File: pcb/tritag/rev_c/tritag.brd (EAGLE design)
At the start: 61 x 34.5 mm, 136 parts, among them J1 TC2030-JLINK-NL, J2 TC2030-JLINK-NL, J3 MICRO_USB_B_HIROSE_ZX62-B-5PA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, J5 BAT_HOLE, J7 CON_MICRO_SDDM3AT-SF-PEJM5, T1 HHM1595A1, U1 NRF52840, U12 SIP32510, U2 MCP73831, U3 FT232RQ, U4 MAX8887EZK33+T, U5 STM32F091CC, U6 SKY13317, U7 LXDC2HN18A, U8 DW1000, U9 LIS2DW12, X1 32MHz, X2 38.4M, X3 16M, X4 32.768kHz

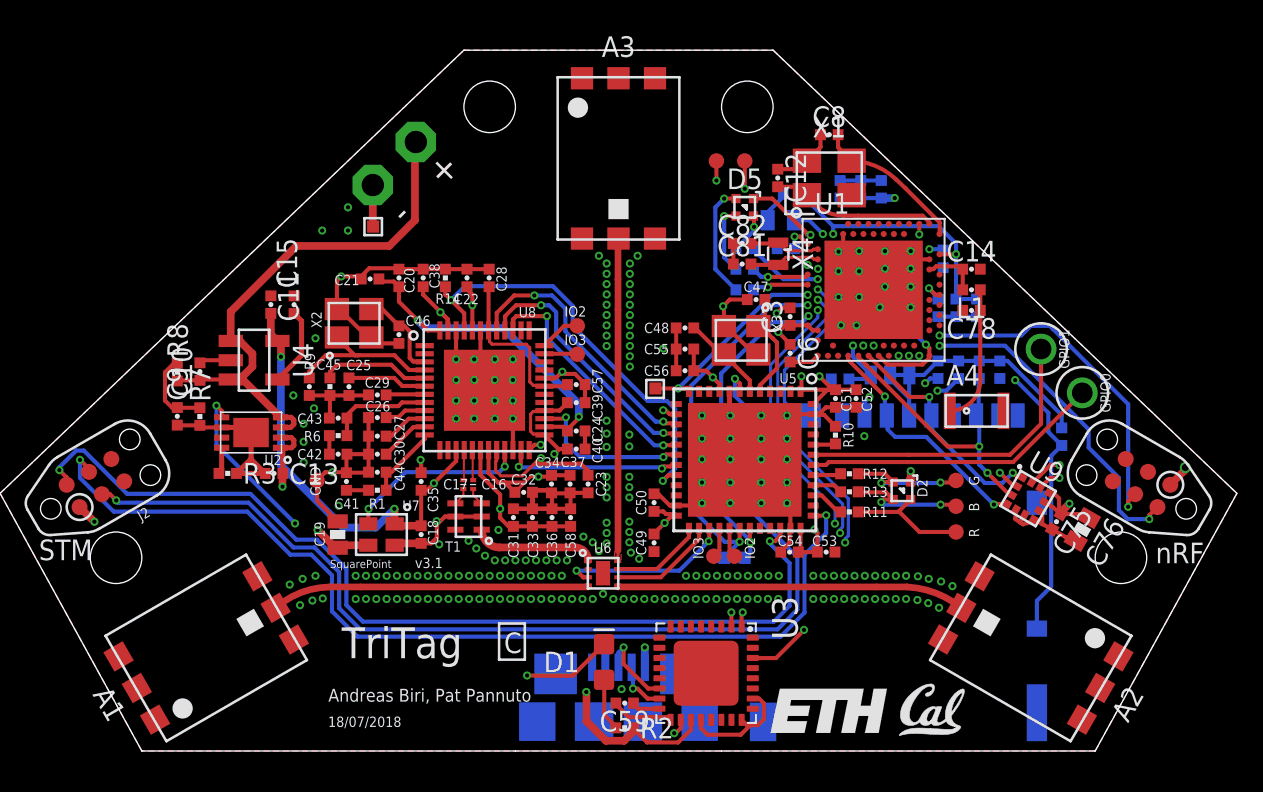
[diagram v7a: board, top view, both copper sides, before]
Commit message: added antenna keepout, improved power distribution and ground coverage plus RF for nRF
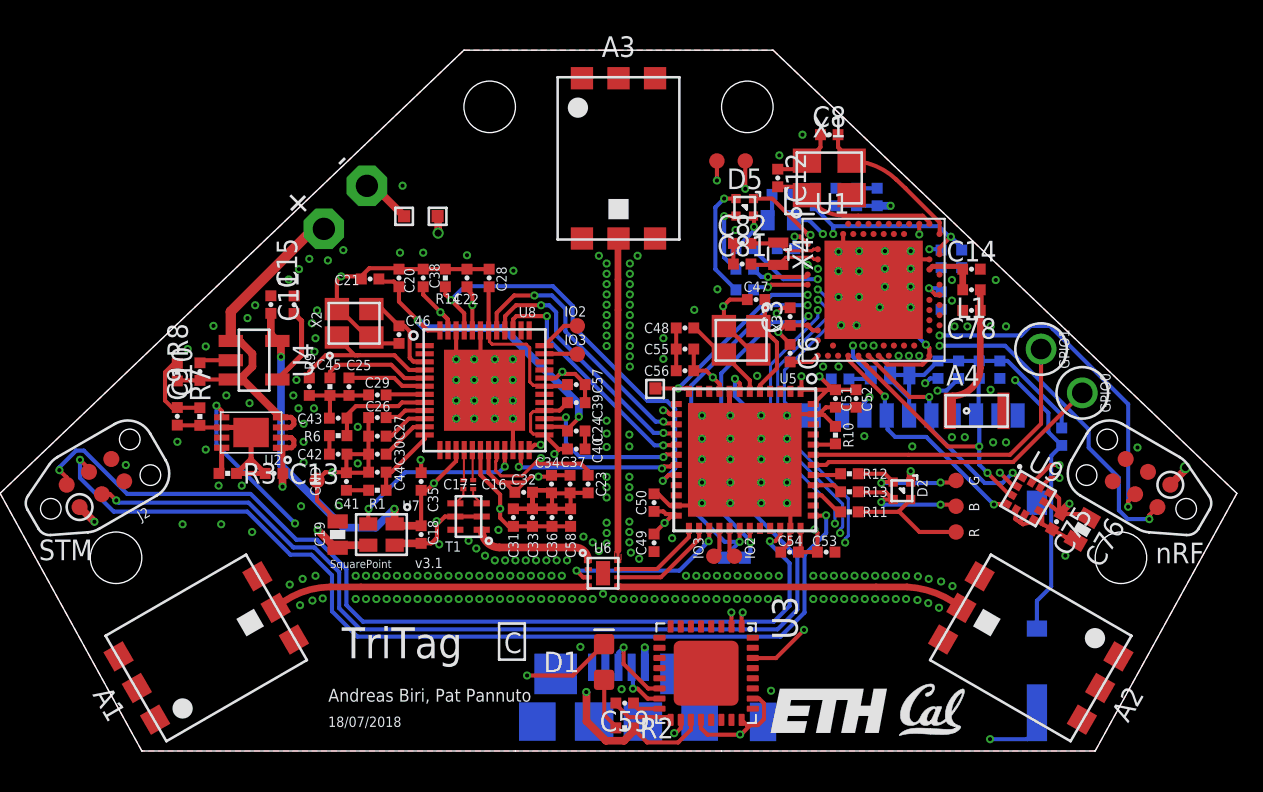
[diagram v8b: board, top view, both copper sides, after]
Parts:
- added TP15: TPTP06SQ, testpad:TP06SQ
- moved C79 9.65 mm to (9.70, 23.5), turned to 90 degrees
- moved J5 3.24 mm to (-13.5, 23.0), turned to 45 degrees
- moved C80 2.43 mm to (16.9, 20.4)
- moved TP4 1.61 mm to (-10.6, 22.5)
- moved L2 0.56 mm to (8.00, 23.6)
- moved C1 0.43 mm to (10.7, 23.5)
- moved C2 0.43 mm to (12.8, 23.5)
- moved C5 0.43 mm to (11.7, 23.5)
- moved C60 0.39 mm to (15.9, 18.4)
- moved C7 0.10 mm to (15.9, 20.4)
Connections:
- net +3V3: now also TP15.TP
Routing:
- net +3V3: track 268.4 -> 287.1 mm, vias 22 -> 23
- net VBAT: track 27.1 -> 18.6 mm
- net N$9: track 13.6 -> 11.8 mm
- net GND: track 152.2 -> 153.3 mm, vias 235 -> 294
- added copper zone on layer 2, net N$28
- added copper zone on layer 2, net N$29
- added copper zone on layer 2, net N$30
